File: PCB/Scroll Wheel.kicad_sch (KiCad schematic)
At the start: 47 parts, among them J1 TC2030, J2 USB_C_Receptacle_USB3.1_16P, J3 Conn_01x02_Pin, J4 Connector Encoder, J5 Connector controller, Q2 BC847, Q3 FDC6318P, SW1 SW_Push, U1 ESP32-WROOM-E, U2 BQ25172DSGR, U6 MIC5504-3.3YM5, U7 AS5600

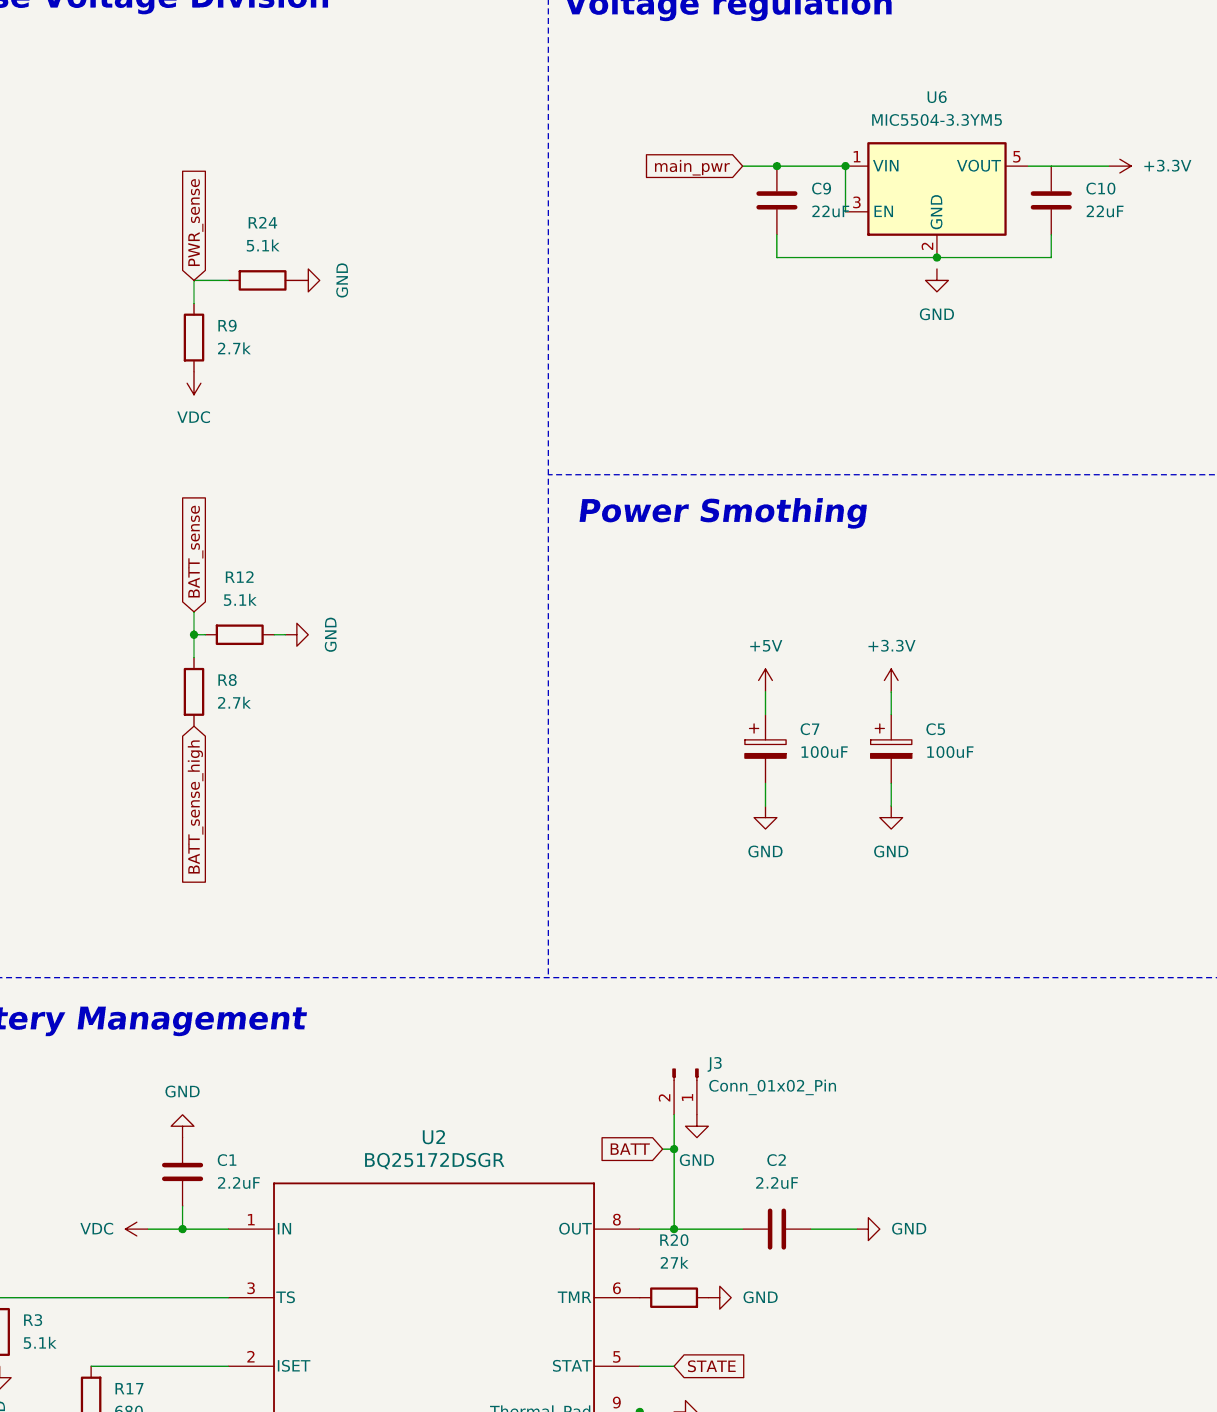
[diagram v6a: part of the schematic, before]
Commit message: change charge controller caps to known value
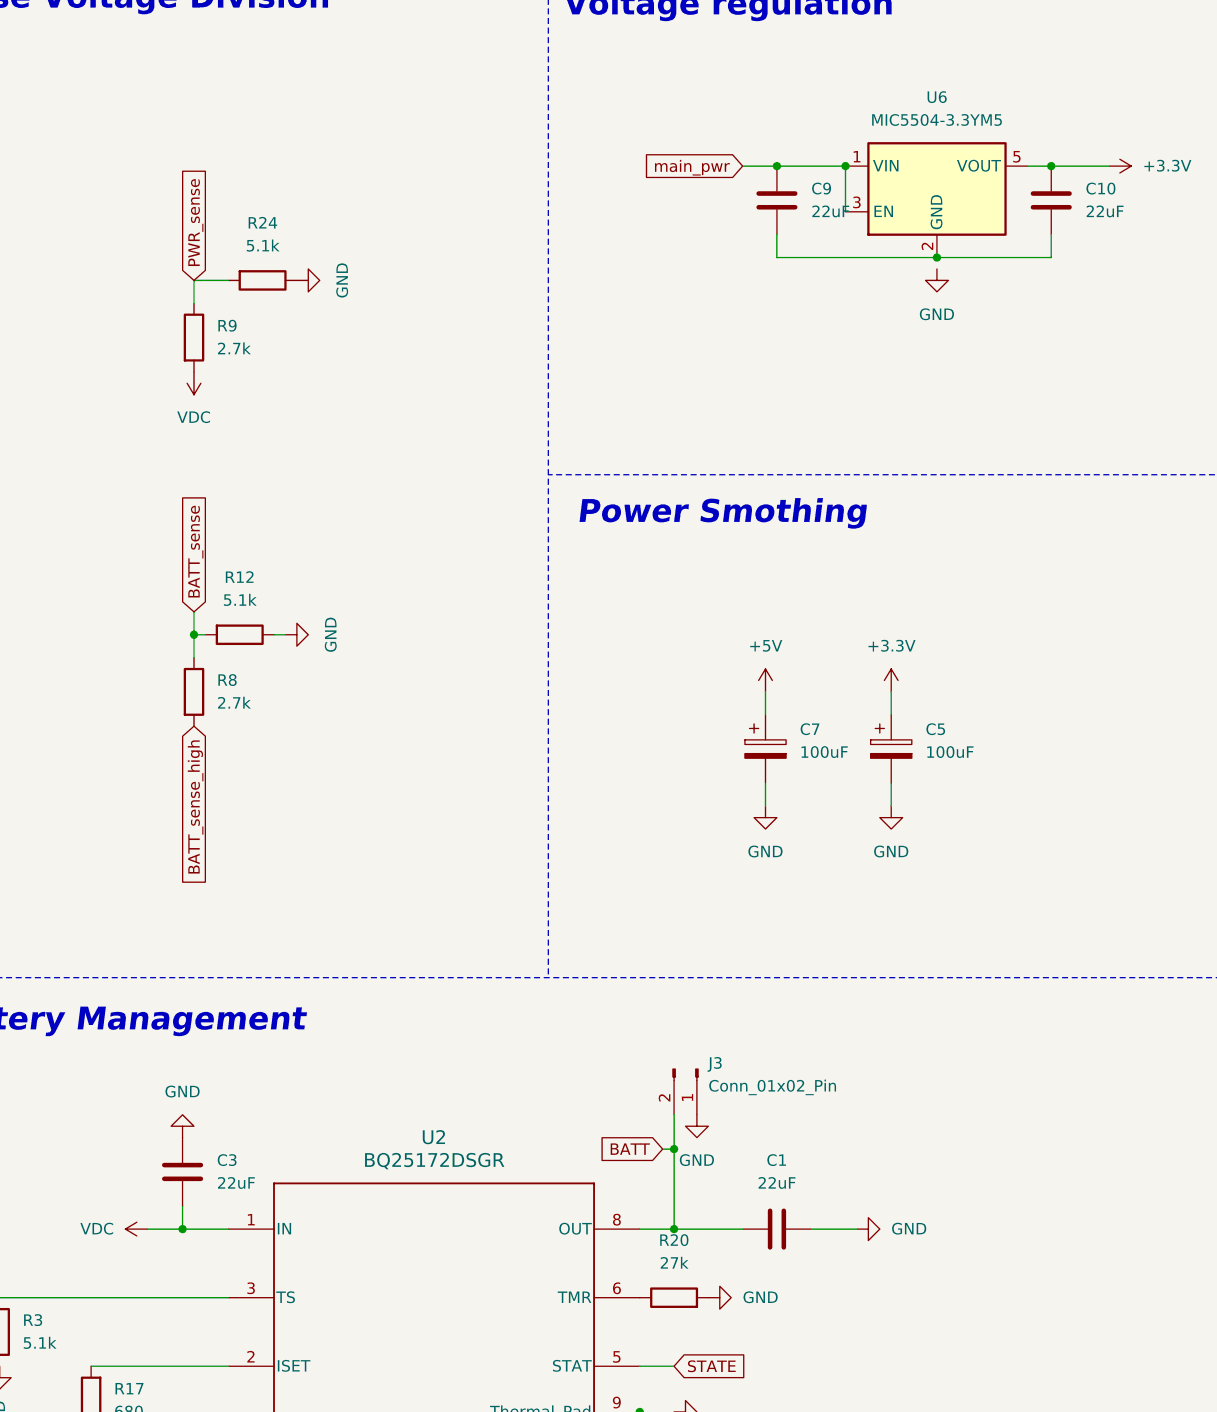
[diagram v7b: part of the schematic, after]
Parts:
- removed C2: 2.2uF, Capacitor_SMD:C_0402_1005Metric, symbol Device:C
- added C3: 22uF, Capacitor_SMD:C_0402_1005Metric, symbol Device:C
- C1: value 2.2uF -> 22uF; LCSC C137948 -> C22367823
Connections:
- net BATT: now also C1.2
- net GND: now also C3.2
- net VDC: now also C3.1; no longer C1.2
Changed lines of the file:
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@@
 	)
 	(junction
+		(at 138.43 118.11)
+		(diameter 0)
+		(color 0 0 0 0)
+	)
+	(junction
 		(at 209.55 215.9)
 		(diameter 0)
@@
 	)
 	(symbol
+		(lib_id "Device:C")
+		(at 41.91 229.87 180)
+		(unit 1)
+		(exclude_from_sim no)
+		(in_bom yes)
+		(on_board yes)
+		(dnp no)
+		(fields_autoplaced yes)
+		(property "Reference" "C3"
+			(at 45.72 228.5999 0)
+			(effects
+				(font
+					(size 1.27 1.27)
+				)
+				(justify right)
+			)
+		)
+		(property "Value" "22uF"
+			(at 45.72 231.1399 0)
+			(effects
+				(font
+					(size 1.27 1.27)
+				)
+				(justify right)
+			)
+		)
+		(property "Footprint" "Capacitor_SMD:C_0402_1005Metric"
+			(at 40.9448 226.06 0)
+			(effects
+				(font
+					(size 1.27 1.27)
+				)
+				(hide yes)
+			)
+		)
+		(property "Datasheet" "~"
+			(at 41.91 229.87 0)
+			(effects
+				(font
+					(size 1.27 1.27)
+				)
+				(hide yes)
+			)
+		)
+		(property "Description" "Unpolarized capacitor"
+			(at 41.91 229.87 0)
+			(effects
+				(font
+					(size 1.27 1.27)
+				)
+				(hide yes)
+			)
+		)
+		(property "LCSC" "C22367823"
+			(at 41.91 229.87 0)
+			(effects
+				(font
+					(size 1.27 1.27)
+				)
+				(hide yes)
+			)
+		)
+		(pin "1"
+		)
+		(pin "2"
+		)
+		(instances
+			(project "Scroll Wheel"
+				(path "/c420c785-f46f-41f2-8236-5ef500ef177b"
+					(reference "C3")
+					(unit 1)
+				)
+			)
+		)
+	)
+	(symbol
 		(lib_id "power:GND")
 		(at 99.06 223.52 0)
@@
 	)
 	(symbol
+		(lib_id "Device:C")
+		(at 107.95 236.22 270)
+		(unit 1)
+		(exclude_from_sim no)
+		(in_bom yes)
+		(on_board yes)
+		(dnp no)
+		(fields_autoplaced yes)
+		(property "Reference" "C1"
+			(at 107.95 228.6 90)
+			(effects
+				(font
+					(size 1.27 1.27)
+				)
+			)
+		)
+		(property "Value" "22uF"
+			(at 107.95 231.14 90)
+			(effects
+				(font
+					(size 1.27 1.27)
+				)
+			)
+		)
+		(property "Footprint" "Capacitor_SMD:C_0402_1005Metric"
+			(at 104.14 237.1852 0)
+			(effects
+				(font
+					(size 1.27 1.27)
+				)
+				(hide yes)
+			)
+		)
+		(property "Datasheet" "~"
+			(at 107.95 236.22 0)
+			(effects
+				(font
+					(size 1.27 1.27)
+				)
+				(hide yes)
+			)
+		)
+		(property "Description" "Unpolarized capacitor"
+			(at 107.95 236.22 0)
+			(effects
+				(font
+					(size 1.27 1.27)
+				)
+				(hide yes)
+			)
+		)
+		(property "LCSC" "C22367823"
+			(at 107.95 236.22 0)
+			(effects
+				(font
+					(size 1.27 1.27)
+				)
+				(hide yes)
+			)
+		)
+		(pin "1"
+		)
+		(pin "2"
+		)
+		(instances
+			(project "Scroll Wheel"
+				(path "/c420c785-f46f-41f2-8236-5ef500ef177b"
+					(reference "C1")
+					(unit 1)
+				)
+			)
+		)
+	)
+	(symbol
 		(lib_id "Connector:TestPoint")
 		(at 261.62 262.89 0)
@@
 					(unit 1)
 				)
-			)
-		)
-	)
-	(symbol
-		(lib_id "Device:C")
-		(at 107.95 236.22 90)
-		(unit 1)
-		(exclude_from_sim no)
-		(in_bom yes)
-		(on_board yes)
-		(dnp no)
-		(fields_autoplaced yes)
-		(property "Reference" "C2"
-			(at 107.95 228.6 90)
-			(effects
-				(font
-					(size 1.27 1.27)
-				)
-			)
-		)
-		(property "Value" "2.2uF"
-			(at 107.95 231.14 90)
-			(effects
-				(font
-					(size 1.27 1.27)
-				)
-			)
-		)
-		(property "Footprint" "Capacitor_SMD:C_0402_1005Metric"
-			(at 111.76 235.2548 0)
-			(effects
-				(font
-					(size 1.27 1.27)
-				)
-				(hide yes)
-			)
-		)
-		(property "Datasheet" "~"
-			(at 107.95 236.22 0)
-			(effects
-				(font
-					(size 1.27 1.27)
-				)
-				(hide yes)
-			)
-		)
-		(property "Description" "Unpolarized capacitor"
-			(at 107.95 236.22 0)
-			(effects
-				(font
-					(size 1.27 1.27)
-				)
-				(hide yes)
-			)
-		)
-		(property "LCSC" "C137948"
-			(at 107.95 236.22 0)
-			(effects
-				(font
-					(size 1.27 1.27)
-				)
-				(hide yes)
-			)
-		)
-		(pin "2"
-		)
-		(pin "1"
-		)
-		(instances
-			(project "Scroll Wheel"
-				(path "/c420c785-f46f-41f2-8236-5ef500ef177b"
-					(reference "C2")
-					(unit 1)
-				)
-			)
-		)
-	)
-	(symbol
-		(lib_id "Device:C")
-		(at 41.91 229.87 0)
-		(unit 1)
-		(exclude_from_sim no)
-		(in_bom yes)
-		(on_board yes)
-		(dnp no)
-		(fields_autoplaced yes)
-		(property "Reference" "C1"
-			(at 45.72 228.5999 0)
-			(effects
-				(font
-					(size 1.27 1.27)
-				)
-				(justify left)
-			)
-		)
-		(property "Value" "2.2uF"
-			(at 45.72 231.1399 0)
-			(effects
-				(font
-					(size 1.27 1.27)
-				)
-				(justify left)
-			)
-		)
-		(property "Footprint" "Capacitor_SMD:C_0402_1005Metric"
-			(at 42.8752 233.68 0)
-			(effects
-				(font
-					(size 1.27 1.27)
-				)
-				(hide yes)
-			)
-		)
-		(property "Datasheet" "~"
-			(at 41.91 229.87 0)
-			(effects
-				(font
-					(size 1.27 1.27)
-				)
-				(hide yes)
-			)
-		)
-		(property "Description" "Unpolarized capacitor"
-			(at 41.91 229.87 0)
-			(effects
-				(font
-					(size 1.27 1.27)
-				)
-				(hide yes)
-			)
-		)
-		(property "LCSC" "C137948"
-			(at 41.91 229.87 0)
-			(effects
-				(font
-					(size 1.27 1.27)
-				)
-				(hide yes)
-			)
-		)
-		(pin "2"
-		)
-		(pin "1"
-		)
-		(instances
-			(project ""
-				(path "/c420c785-f46f-41f2-8236-5ef500ef177b"
-					(reference "C1")
-					(unit 1)
-				)

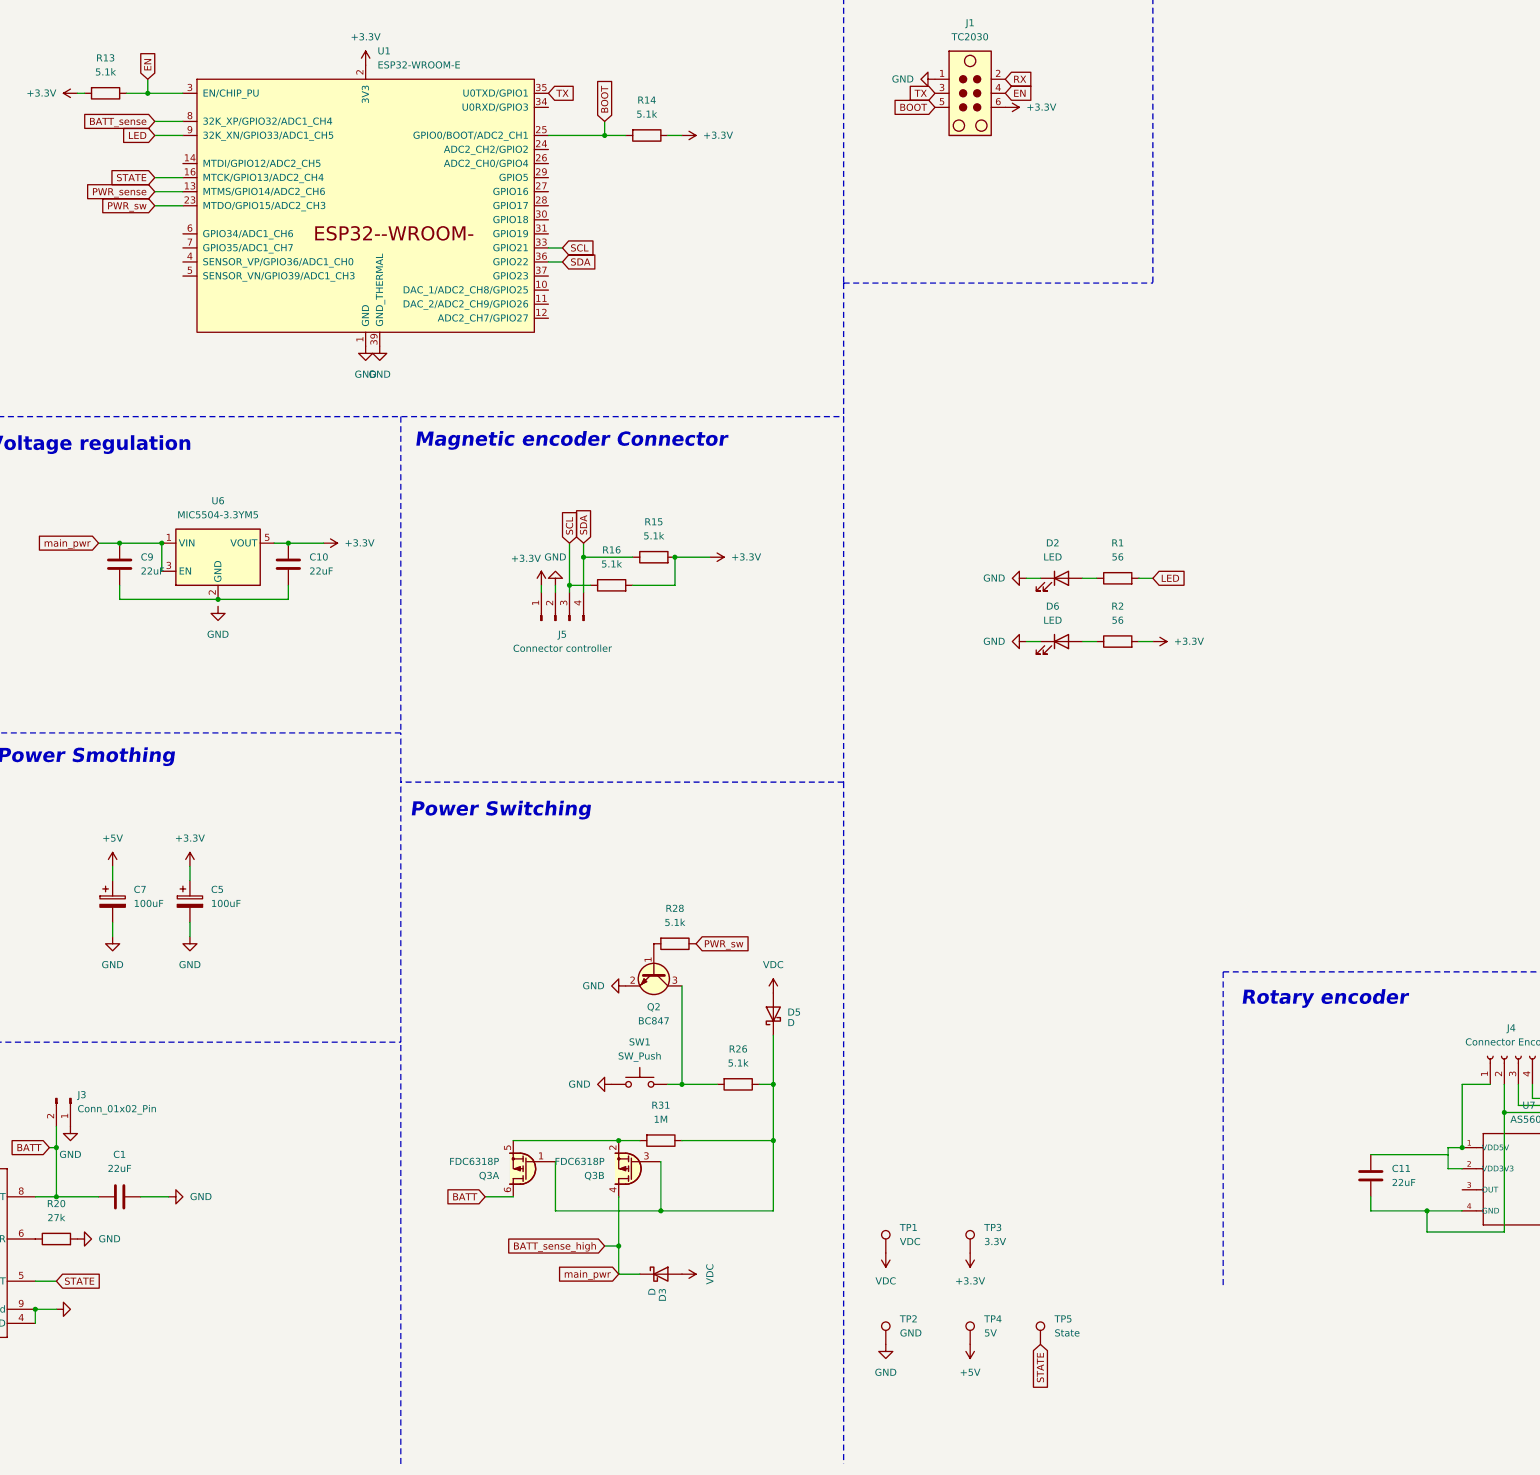
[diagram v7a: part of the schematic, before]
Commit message: Complete rerouting, fixing all open issues #6 #2 #1
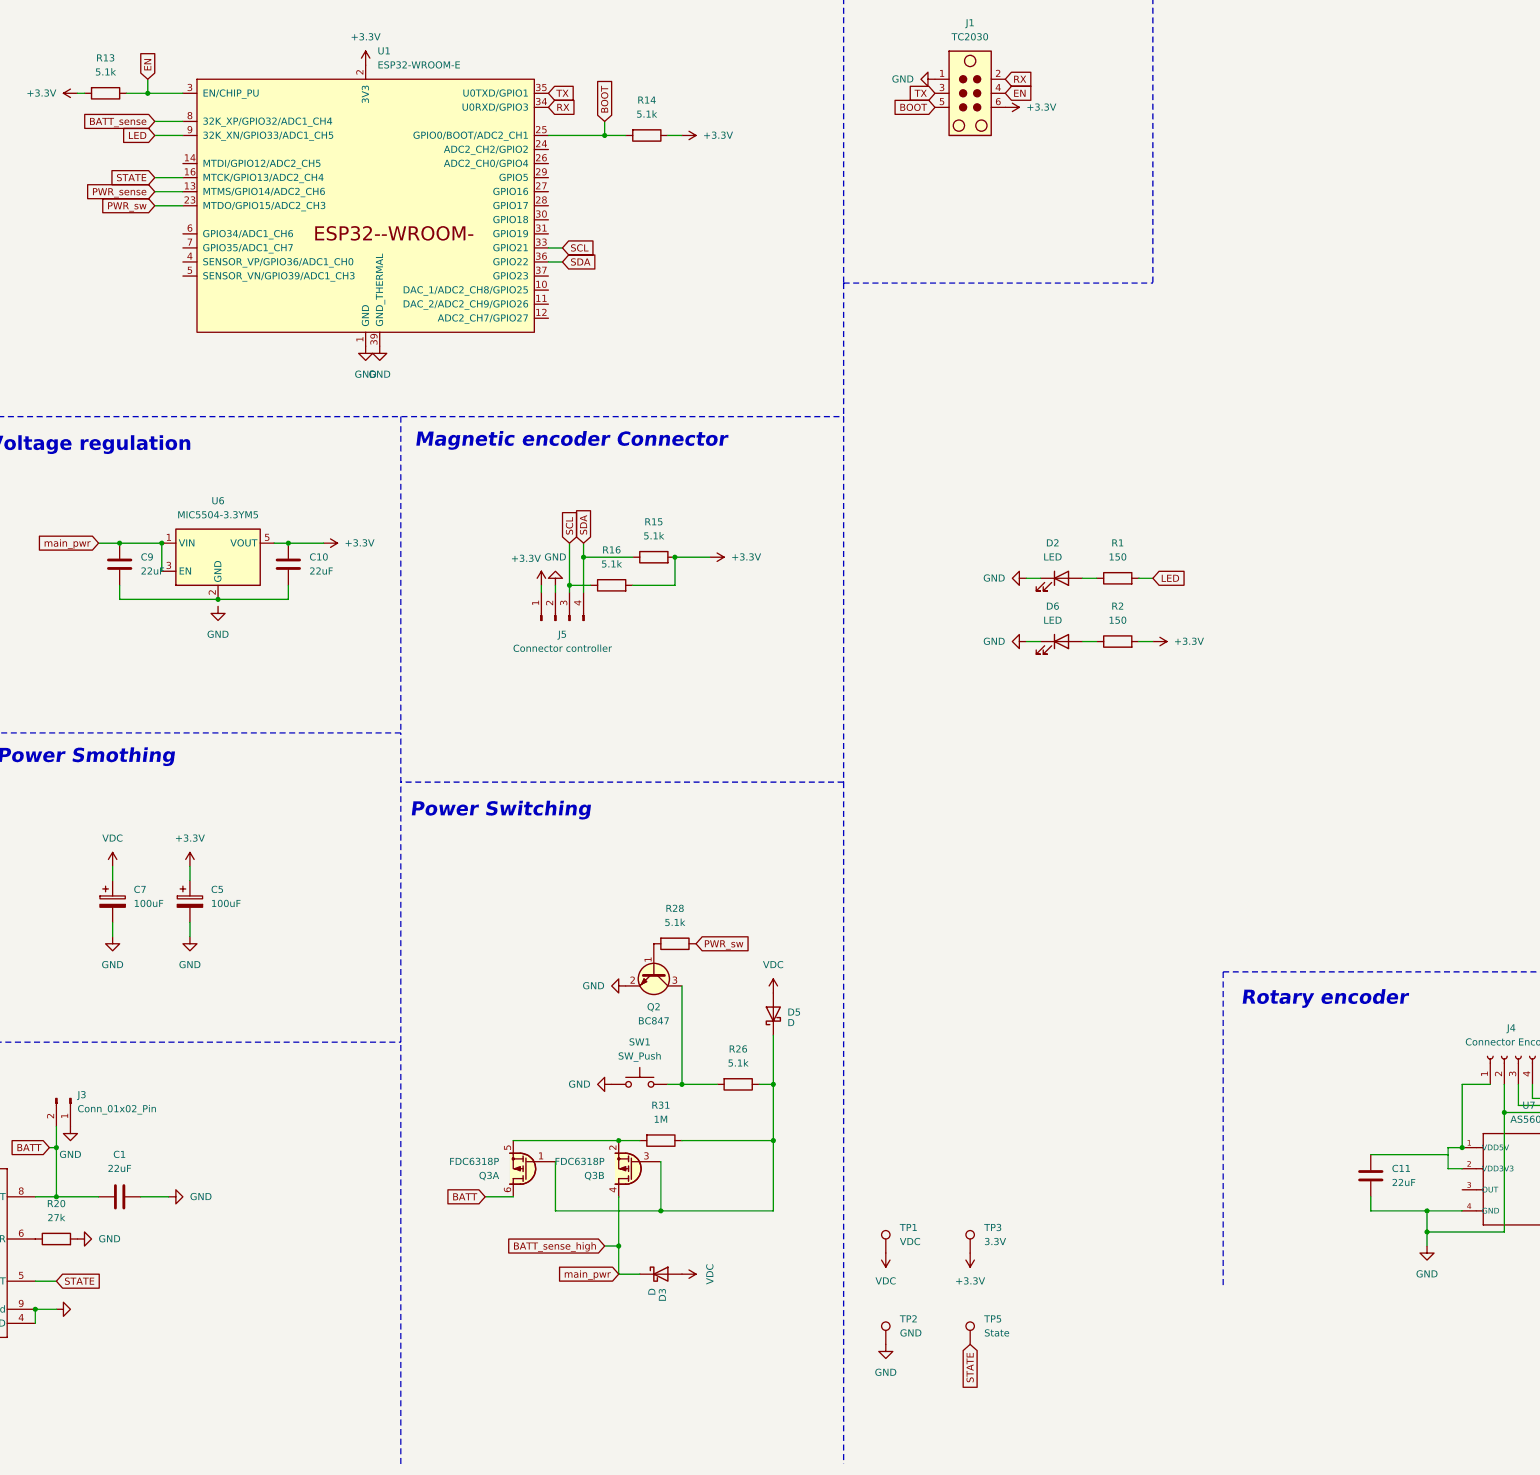
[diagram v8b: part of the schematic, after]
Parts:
- removed TP4: 5V, TestPoint:TestPoint_Pad_D1.0mm, symbol Connector:TestPoint
- R1, R2: value 56 -> 150; LCSC C25744 -> C138054
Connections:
- net +5V is gone; now on net VDC: C7.1
- net GND: now also C11.1, J4.2 (Pin_2), U7.4 (GND), U7.8 (DIR)
- net RX: now also U1.34 (U0RXD/GPIO3)
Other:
- moved on the sheet: TP5
